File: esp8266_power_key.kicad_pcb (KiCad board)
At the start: 2 copper layers, 59.7 x 23.2 mm, 32 parts, among them P1 CONN_01X02, P2 CONN_01X02, P3 CONN_01X02, Q1 Q_NMOS_SDG, Q2 Q_NMOS_SDG, Q4 BC849, Q6 BC849, U1 ESP-01v090, U2 LP2988AIMX-3.3/NOPB

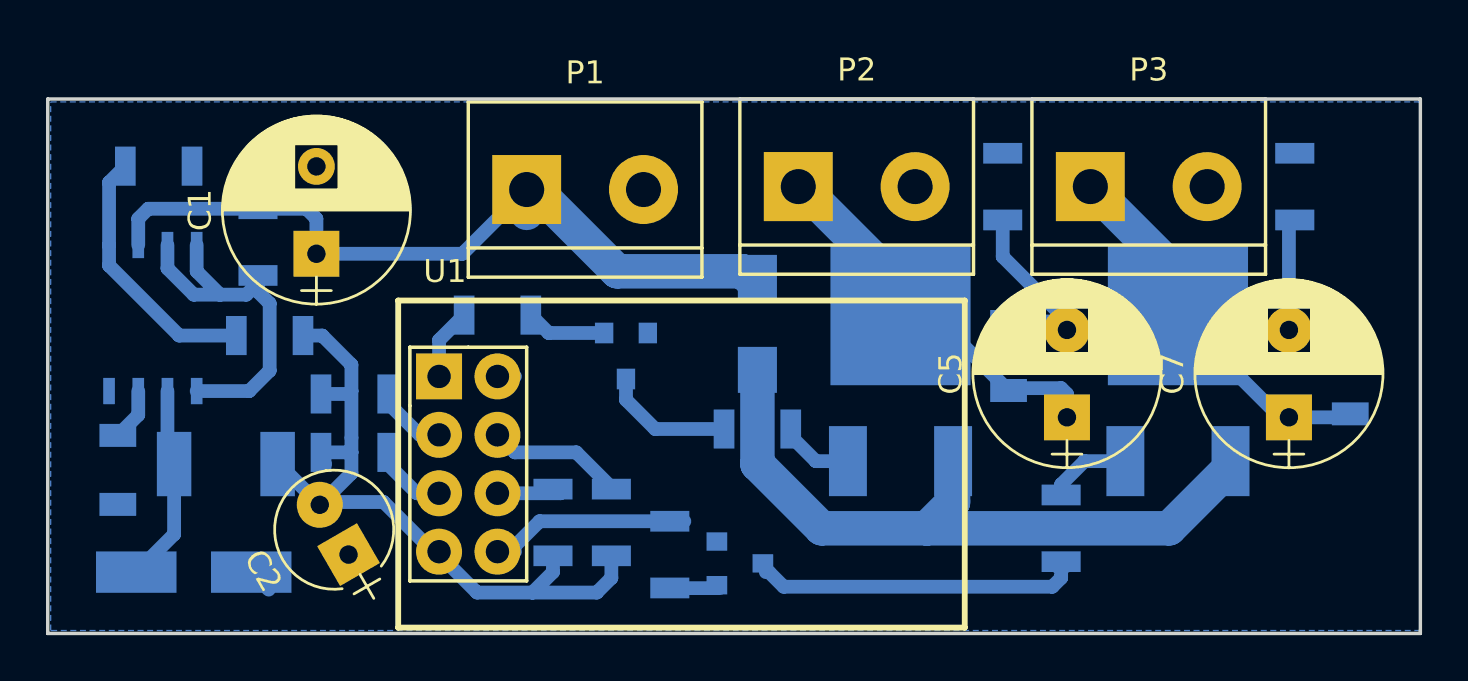
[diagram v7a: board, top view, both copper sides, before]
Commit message: topology fix
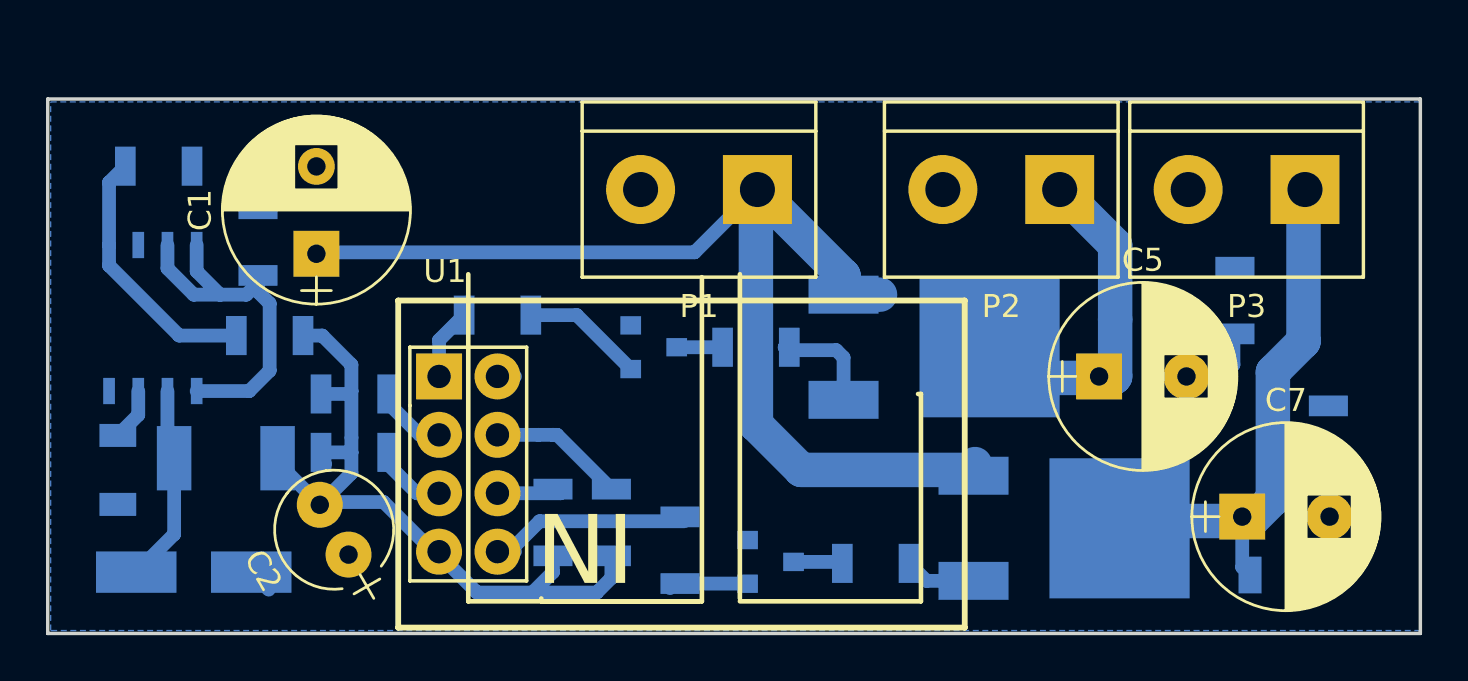
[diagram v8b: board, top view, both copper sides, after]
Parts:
- removed R14: R, Resistors_SMD:R_1206_HandSoldering
- Q1, Q2: value Q_NMOS_SDG -> Q_NMOS_GDS
- moved R5 11.2 mm to (113.9, 68.6)
- moved R9 11.1 mm to (117.9, 74.6)
- moved Q2 9.36 mm to (102.5, 78.5), turned to 90 degrees
- moved C6 8.98 mm to (116.0, 80.5), turned to 180 degrees
- moved R12 8.21 mm to (98.2, 80.0), turned to 180 degrees
- moved C4 6.44 mm to (110.2, 69.3), turned to 180 degrees
- moved P2 6.29 mm to (103.7, 63.8), turned to 180 degrees
- moved Q1 5.54 mm to (96.8, 70.6), turned to 90 degrees
- moved P1 4.95 mm to (90.6, 63.8), turned to 180 degrees
- moved C7 4.77 mm to (114.2, 78.0), turned to 0 degrees
- moved P3 4.26 mm to (114.4, 63.8), turned to 180 degrees
- moved R4 3.56 mm to (93.0, 70.6)
- moved C5 2.26 mm to (108.0, 71.9), turned to 0 degrees
- moved Q6 1.34 mm to (93.7, 79.9)
- moved Q4 1.27 mm to (88.6, 70.6), turned to 0 degrees
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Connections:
- Q1 pad 3: Net-(Q1-Pad3) -> +36V
- Q2 pad 1: Net-(Q1-Pad1) -> Net-(Q2-Pad1)
- Q2 pad 3: Net-(Q2-Pad3) -> +36V
- R12 pad 1: Net-(Q2-Pad3) -> Net-(Q2-Pad1)
- R4 pad 1: Net-(Q1-Pad3) -> Net-(Q1-Pad1)
- R6 pad 2: +36V -> Net-(R6-Pad2)
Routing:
- net Net-(Q1-Pad1): track 30.5 -> 4.79 mm
- net +36V: track 33.9 -> 48.3 mm
- net Net-(Q6-Pad3): track 14.6 -> 2.15 mm
- net Net-(C6-Pad2): track 16.9 -> 26.0 mm
- net Net-(Q4-Pad3): track 5.70 -> 2.00 mm
- net Net-(Q2-Pad3): track 3.67 -> 0.00 mm
- net Net-(Q1-Pad3): track 3.25 -> 0.00 mm
- net Net-(Q2-Pad1): track 0.00 -> 3.12 mm
- net Net-(C6-Pad1): track 7.70 -> 4.67 mm
- net Net-(C4-Pad1): track 8.63 -> 5.64 mm
- net Net-(C4-Pad2): track 17.8 -> 15.2 mm
- net Net-(Q4-Pad1): track 3.51 -> 5.32 mm
- net Net-(Q6-Pad1): track 2.18 -> 2.95 mm
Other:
- board text added: "IN"
